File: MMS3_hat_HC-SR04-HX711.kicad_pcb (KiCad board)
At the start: 2 copper layers, 100 x 50 mm, 21 parts, among them J1 Chainbus in, J2 Chainbus Out, J3 Conn_01x04_Pin, U1 SN74CB3Q3384APW, U2 M24C64

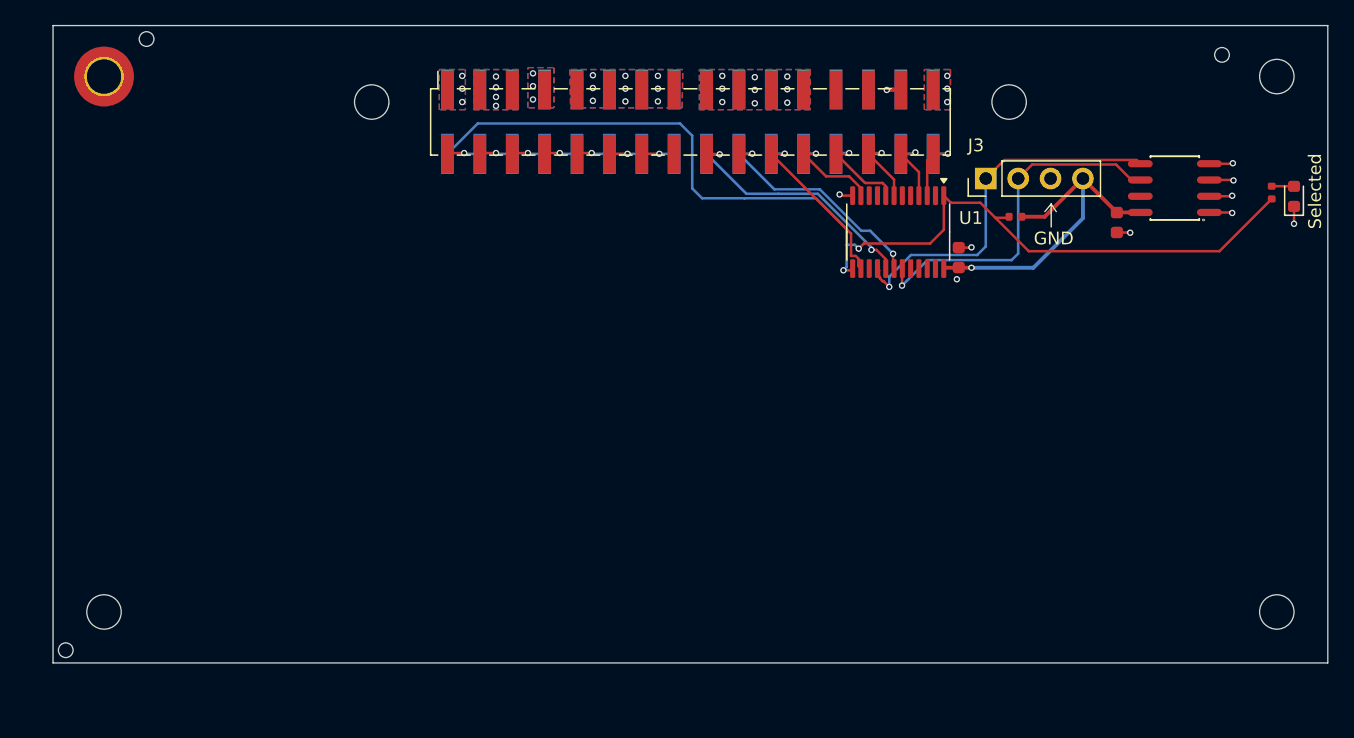
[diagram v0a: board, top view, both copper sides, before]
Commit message: finished routing and exported gerber
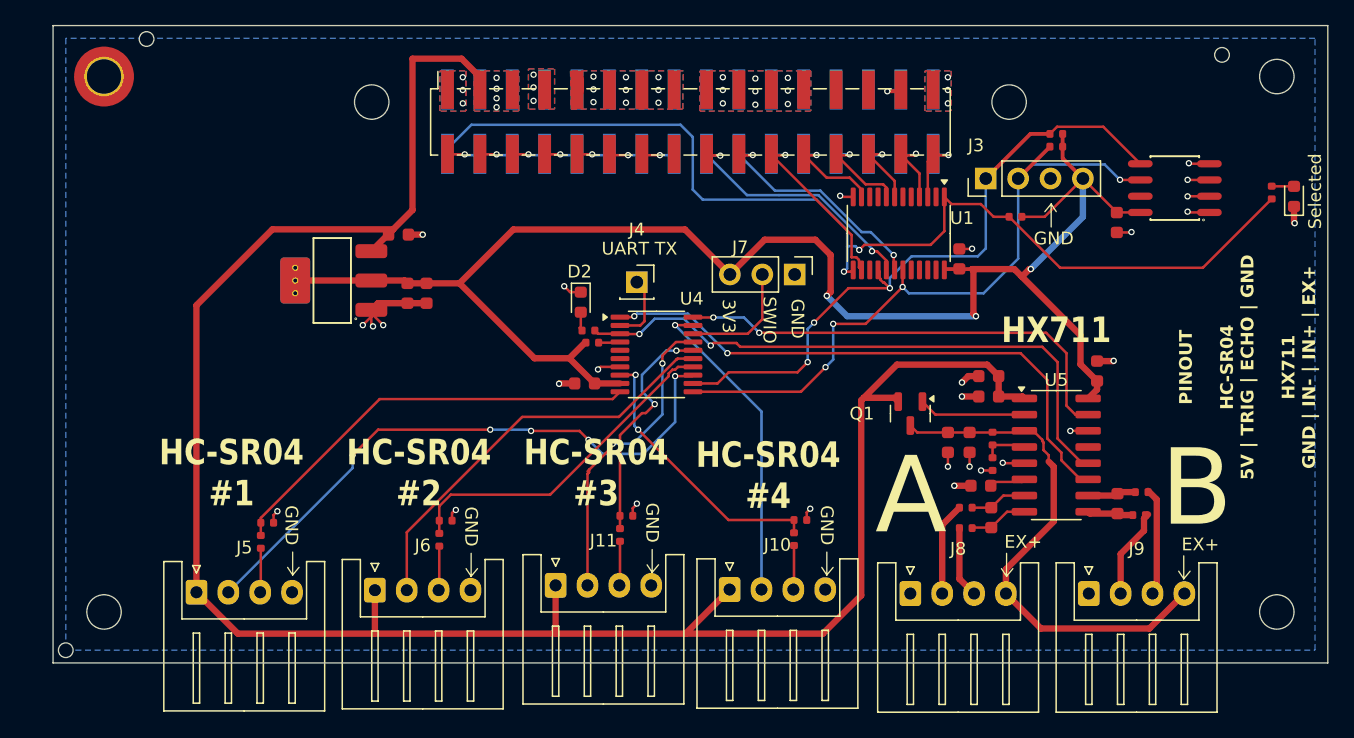
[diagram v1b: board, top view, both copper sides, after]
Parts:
- added C10: 100nF, PCM_JLCPCB:C_0603, F.Cu at (161.5, 125.5)
- added C11: 10uF, PCM_JLCPCB:C_0603, F.Cu at (148.2, 120.7)
- added C12: 100nF, PCM_JLCPCB:C_0603, F.Cu at (149.9, 120.7)
- added C13: 100nF, PCM_JLCPCB:C_0603, F.Cu at (150.8, 124.1)
- added C14: 10uF, PCM_JLCPCB:C_0603, F.Cu at (151.4, 115.5)
- added C15: 100nF, PCM_JLCPCB:C_0603, F.Cu at (151.4, 117.1)
- added C16: 100nF, PCM_JLCPCB:C_0603, F.Cu at (159.9, 115.1)
- added C3: 10uF, PCM_JLCPCB:C_0603, F.Cu at (105.1, 104.4)
- added C4: 10uF, PCM_JLCPCB:C_0603, F.Cu at (107.3, 109.0)
- added C5: 10uF, PCM_JLCPCB:C_0603, F.Cu at (105.8, 109.0)
- added C6: 100nF, PCM_JLCPCB:C_0603, F.Cu at (119.7, 116.1)
- added C9: 100nF, PCM_JLCPCB:C_0603, F.Cu at (151.6, 126.6)
- added D2: LED, LED_SMD:LED_0603_1608Metric, F.Cu at (119.4, 109.7)
- added J10: Conn_01x04_Pin, Connector_JST:JST_XH_S4B-XH-A_1x04_P2.50mm_Horizontal, F.Cu at (131.1, 132.2)
- added J11: Conn_01x04_Pin, Connector_JST:JST_XH_S4B-XH-A_1x04_P2.50mm_Horizontal, F.Cu at (117.4, 131.9)
- added J4: Debug_USART_TX, Connector_PinSocket_2.54mm:PinSocket_1x01_P2.54mm_Vertical, F.Cu at (123.8, 108.1)
- added J5: Conn_01x04_Pin, Connector_JST:JST_XH_S4B-XH-A_1x04_P2.50mm_Horizontal, F.Cu at (89.2, 132.5)
- added J6: Conn_01x04_Pin, Connector_JST:JST_XH_S4B-XH-A_1x04_P2.50mm_Horizontal, F.Cu at (103.2, 132.3)
- added J7: Program, Connector_PinHeader_2.54mm:PinHeader_1x03_P2.54mm_Vertical, F.Cu at (136.2, 107.5)
- added J8: Conn_01x04_Pin, Connector_JST:JST_XH_S4B-XH-A_1x04_P2.50mm_Horizontal, F.Cu at (145.2, 132.6)
- added J9: Conn_01x04_Pin, Connector_JST:JST_XH_S4B-XH-A_1x04_P2.50mm_Horizontal, F.Cu at (159.2, 132.6)
- added Q1: MMBT3906, Package_TO_SOT_SMD:SOT-23, F.Cu at (145.2, 118.4)
- added R11: 10kΩ, PCM_JLCPCB:R_0402, F.Cu at (120.3, 112.9)
- added R12: 330Ω, PCM_JLCPCB:R_0402, F.Cu at (120.0, 111.9)
- added R13: 100Ω, PCM_JLCPCB:R_0402, F.Cu at (149.6, 127.4)
- added R14: 100Ω, PCM_JLCPCB:R_0402, F.Cu at (149.6, 125.8)
- added R15: 100Ω, PCM_JLCPCB:R_0402, F.Cu at (163.2, 126.4)
- added R16: 100Ω, PCM_JLCPCB:R_0402, F.Cu at (163.4, 124.6)
- added R17: 20kΩ, PCM_JLCPCB:R_0402, F.Cu at (151.7, 120.4)
- added R18: 8.2kΩ, PCM_JLCPCB:R_0402, F.Cu at (151.7, 122.4)
- added R19: 10kΩ, PCM_JLCPCB:R_0402, F.Cu at (136.1, 128.3)
- added R2: 10kΩ, PCM_JLCPCB:R_0402, F.Cu at (156.7, 97.5)
- added R20: 15kΩ, PCM_JLCPCB:R_0402, F.Cu at (136.6, 126.8)
- added R21: 10kΩ, PCM_JLCPCB:R_0402, F.Cu at (122.5, 128.0)
- added R22: 15kΩ, PCM_JLCPCB:R_0402, F.Cu at (123.0, 126.5)
- added R3: 10kΩ, PCM_JLCPCB:R_0402, F.Cu at (156.7, 96.5)
- added R5: 10kΩ, PCM_JLCPCB:R_0402, F.Cu at (94.3, 128.5)
- added R6: 15kΩ, PCM_JLCPCB:R_0402, F.Cu at (94.8, 127.0)
- added R7: 10kΩ, PCM_JLCPCB:R_0402, F.Cu at (108.3, 128.3)
- added R8: 15kΩ, PCM_JLCPCB:R_0402, F.Cu at (108.8, 126.8)
- added U3: AMS1117, PCM_JLCPCB:SOT-223-3_L6.5-W3.4-P2.30-LS7.0-BR, F.Cu at (100.0, 108.0)
- added U4: CH32V003FxPx, Package_SO:TSSOP-20_4.4x6.5mm_P0.65mm, F.Cu at (125.3, 113.8)
- added U5: HX711, Package_SO:SOP-16_3.9x9.9mm_P1.27mm, F.Cu at (156.7, 121.7)
- moved C1 0.11 mm to (149.1, 106.3)
- moved U1 0.11 mm to (144.3, 104.3)
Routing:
- net +5V: track 0.00 -> 164.7 mm
- net +3V3: track 27.3 -> 128.3 mm, vias 1 -> 3
- net /CH32V003/PC3: track 0.00 -> 47.9 mm, vias 0 -> 5
- net /CH32V003/CH32V003.RX: track 0.00 -> 47.7 mm, vias 0 -> 2
- net /CH32V003/PD4: track 0.00 -> 45.3 mm, vias 0 -> 2
- net /HX711/EX+: track 0.00 -> 41.2 mm
- net /CH32V003/PD3: track 0.00 -> 36.6 mm, vias 0 -> 2
- net /CH32V003/PC0: track 0.00 -> 33.7 mm
- net /CH32V003/CH32V003.SCK: track 0.00 -> 32.6 mm
- net GND: track 12.1 -> 41.9 mm, vias 27 -> 46
- net /CH32V003/PC4: track 0.00 -> 26.7 mm
- net /Bus_switch/Chainbus.SCL: track 27.9 -> 53.6 mm, vias 1 -> 4
- net /CH32V003/PD2: track 0.00 -> 25.0 mm, vias 0 -> 1
- net /CH32V003/CH32V003.MISO: track 0.00 -> 24.4 mm, vias 0 -> 2
- net /Bus_switch/Chainbus.SDA: track 29.4 -> 51.7 mm, vias 1 -> 3
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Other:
- board text added: "3V3"
- board text added: "A"
- board text added: "B"
- board text added: "EX+"
- board text added: "HC-SR04 #1"
- board text added: "HC-SR04 #2"
- board text added: "HC-SR04 #3"
- board text added: "HC-SR04 #4"
- board text added: "HX711"
- board text added: "PINOUT HC-SR04 5V | TRIG | ECHO | GND HX711 GND | IN- | IN+ | EX+"
- board text added: "SWIO"
- board text added: "UART TX"

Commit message: Added version number
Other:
- board text added: "Version 1.0 Wojciech Szafrański"
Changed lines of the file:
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@@
+		)
+	)
+	(gr_text "Version 1.0\nWojciech Szafrański"
+		(at 92.5 98.25 0)
+		(layer "F.SilkS")
+		(effects
+			(font
+				(size 2 1.7)
+				(thickness 0.3)
+				(bold yes)
+			)
 		)
 	)
